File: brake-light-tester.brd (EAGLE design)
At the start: 47.2 x 62.2 mm, 24 parts, among them J1 CON_HEADER_PRG_AVR_ICSP-SMD, U1 ATTINY85-20SU, U2 TSL2561FN, U4 LM1117/5V

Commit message: Final version with silkscreens.
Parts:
- moved FID2 4.02 mm to (56.1, 28.9)
- moved FID1 1.27 mm to (22.9, 49.5)
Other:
- board text added: "(c) Chris von Csefalvay"
- board text added: "0x49 0x39 0x29"
- board text added: "BrakeDancer Mk I"
- board text added: "CR927 x 3"
- board text added: "Firmware"
- board text added: "Mfg: Date: S/N: Line: Batch: 20 19 18 17 16"

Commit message: Added drill legend.
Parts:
- added DRILEGEND: (no value), drilegend:DRILEGEND
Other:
- board text added: "01-16"
- board text added: "LAYER-STACK"
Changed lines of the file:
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@@
 <layer number="131" name="tAdjust" color="7" fill="1" visible="no" active="yes"/>
 <layer number="132" name="bAdjust" color="7" fill="1" visible="no" active="yes"/>
-<layer number="144" name="Drill_legend" color="7" fill="1" visible="no" active="yes"/>
+<layer number="144" name="DrillLegend" color="7" fill="1" visible="yes" active="yes"/>
+<layer number="145" name="DrillLegend_01-16" color="2" fill="9" visible="yes" active="yes"/>
 <layer number="150" name="Notes" color="7" fill="1" visible="no" active="yes"/>
 <layer number="151" name="HeatSink" color="7" fill="1" visible="no" active="yes"/>
@@
 <text x="46.99" y="15.24" size="0.6096" layer="122" font="vector" ratio="4">Firmware</text>
 <rectangle x1="41.91" y1="8.89" x2="55.88" y2="13.97" layer="122"/>
+<text x="-13.994165625" y="-10.905" size="0.6096" layer="144" font="vector" ratio="4">LAYER-STACK</text>
+<text x="-4.215165625" y="-13.8387" size="1.778" layer="145" font="vector" ratio="4">01-16</text>
+<wire x1="20.32" y1="29.718" x2="20.32" y2="28.702" width="0.1016" layer="145"/>
+<wire x1="19.812" y1="29.21" x2="20.828" y2="29.21" width="0.1016" layer="145"/>
+<wire x1="20.32" y1="37.338" x2="20.32" y2="36.322" width="0.1016" layer="145"/>
+<wire x1="19.812" y1="36.83" x2="20.828" y2="36.83" width="0.1016" layer="145"/>
+<wire x1="41.91" y1="39.878" x2="41.91" y2="38.862" width="0.1016" layer="145"/>
+<wire x1="41.402" y1="39.37" x2="42.418" y2="39.37" width="0.1016" layer="145"/>
+<wire x1="40.64" y1="48.768" x2="40.64" y2="47.752" width="0.1016" layer="145"/>
+<wire x1="40.132" y1="48.26" x2="41.148" y2="48.26" width="0.1016" layer="145"/>
+<wire x1="45.72" y1="36.068" x2="45.72" y2="35.052" width="0.1016" layer="145"/>
+<wire x1="45.212" y1="35.56" x2="46.228" y2="35.56" width="0.1016" layer="145"/>
+<wire x1="34.29" y1="34.798" x2="34.29" y2="33.782" width="0.1016" layer="145"/>
+<wire x1="33.782" y1="34.29" x2="34.798" y2="34.29" width="0.1016" layer="145"/>
+<wire x1="26.67" y1="37.338" x2="26.67" y2="36.322" width="0.1016" layer="145"/>
+<wire x1="26.162" y1="36.83" x2="27.178" y2="36.83" width="0.1016" layer="145"/>
+<wire x1="46.99" y1="30.988" x2="46.99" y2="29.972" width="0.1016" layer="145"/>
+<wire x1="46.482" y1="30.48" x2="47.498" y2="30.48" width="0.1016" layer="145"/>
+<wire x1="33.02" y1="36.068" x2="33.02" y2="35.052" width="0.1016" layer="145"/>
+<wire x1="32.512" y1="35.56" x2="33.528" y2="35.56" width="0.1016" layer="145"/>
+<wire x1="34.29" y1="47.498" x2="34.29" y2="46.482" width="0.1016" layer="145"/>
+<wire x1="33.782" y1="46.99" x2="34.798" y2="46.99" width="0.1016" layer="145"/>
+<wire x1="52.07" y1="24.638" x2="52.07" y2="23.622" width="0.1016" layer="145"/>
+<wire x1="51.562" y1="24.13" x2="52.578" y2="24.13" width="0.1016" layer="145"/>
+<wire x1="41.91" y1="28.448" x2="41.91" y2="27.432" width="0.1016" layer="145"/>
+<wire x1="41.402" y1="27.94" x2="42.418" y2="27.94" width="0.1016" layer="145"/>
+<wire x1="49.53" y1="24.638" x2="49.53" y2="23.622" width="0.1016" layer="145"/>
+<wire x1="49.022" y1="24.13" x2="50.038" y2="24.13" width="0.1016" layer="145"/>
+<wire x1="48.635684375" y1="27.178" x2="48.635684375" y2="26.162" width="0.1016" layer="145"/>
+<wire x1="48.127684375" y1="26.67" x2="49.143684375" y2="26.67" width="0.1016" layer="145"/>
+<wire x1="41.91" y1="43.688" x2="41.91" y2="42.672" width="0.1016" layer="145"/>
+<wire x1="41.402" y1="43.18" x2="42.418" y2="43.18" width="0.1016" layer="145"/>
+<wire x1="48.26" y1="42.418" x2="48.26" y2="41.402" width="0.1016" layer="145"/>
+<wire x1="47.752" y1="41.91" x2="48.768" y2="41.91" width="0.1016" layer="145"/>
+<wire x1="39.37" y1="33.528" x2="39.37" y2="32.512" width="0.1016" layer="145"/>
+<wire x1="38.862" y1="33.02" x2="39.878" y2="33.02" width="0.1016" layer="145"/>
+<wire x1="36.83" y1="46.228" x2="36.83" y2="45.212" width="0.1016" layer="145"/>
+<wire x1="36.322" y1="45.72" x2="37.338" y2="45.72" width="0.1016" layer="145"/>
+<wire x1="36.83" y1="33.528" x2="36.83" y2="32.512" width="0.1016" layer="145"/>
+<wire x1="36.322" y1="33.02" x2="37.338" y2="33.02" width="0.1016" layer="145"/>
+<wire x1="39.37" y1="55.118" x2="39.37" y2="54.102" width="0.1016" layer="145"/>
+<wire x1="38.862" y1="54.61" x2="39.878" y2="54.61" width="0.1016" layer="145"/>
+<wire x1="39.37" y1="34.798" x2="39.37" y2="33.782" width="0.1016" layer="145"/>
+<wire x1="38.862" y1="34.29" x2="39.878" y2="34.29" width="0.1016" layer="145"/>
+<wire x1="41.45579375" y1="32.45383125" x2="41.45579375" y2="31.43783125" width="0.1016" layer="145"/>
+<wire x1="40.94779375" y1="31.94583125" x2="41.96379375" y2="31.94583125" width="0.1016" layer="145"/>
+<wire x1="38.1" y1="53.848" x2="38.1" y2="52.832" width="0.1016" layer="145"/>
+<wire x1="37.592" y1="53.34" x2="38.608" y2="53.34" width="0.1016" layer="145"/>
+<wire x1="38.455309375" y1="38.761453125" x2="38.455309375" y2="37.745453125" width="0.1016" layer="145"/>
+<wire x1="37.947309375" y1="38.253453125" x2="38.963309375" y2="38.253453125" width="0.1016" layer="145"/>
+<wire x1="30.48" y1="41.148" x2="30.48" y2="40.132" width="0.1016" layer="145"/>
+<wire x1="29.972" y1="40.64" x2="30.988" y2="40.64" width="0.1016" layer="145"/>
+<wire x1="27.94" y1="41.148" x2="27.94" y2="40.132" width="0.1016" layer="145"/>
+<wire x1="27.432" y1="40.64" x2="28.448" y2="40.64" width="0.1016" layer="145"/>
+<wire x1="22.352" y1="56.388" x2="23.368" y2="55.372" width="0.1016" layer="145"/>
+<wire x1="23.368" y1="56.388" x2="22.352" y2="55.372" width="0.1016" layer="145"/>
+<wire x1="27.432" y1="6.858" x2="28.448" y2="5.842" width="0.1016" layer="145"/>
+<wire x1="28.448" y1="6.858" x2="27.432" y2="5.842" width="0.1016" layer="145"/>
 </plain>
 <attributes>
@@
 <attribute name="VALUE" x="23.495" y="28.194" size="0.4064" layer="27" ratio="10" rot="R270"/>
 </element>
+<element name="DRILEGEND" library="drilegend" package="DRILEGEND" value="" x="4.67484375" y="-10.90500625"/>
 </elements>
 <signals>

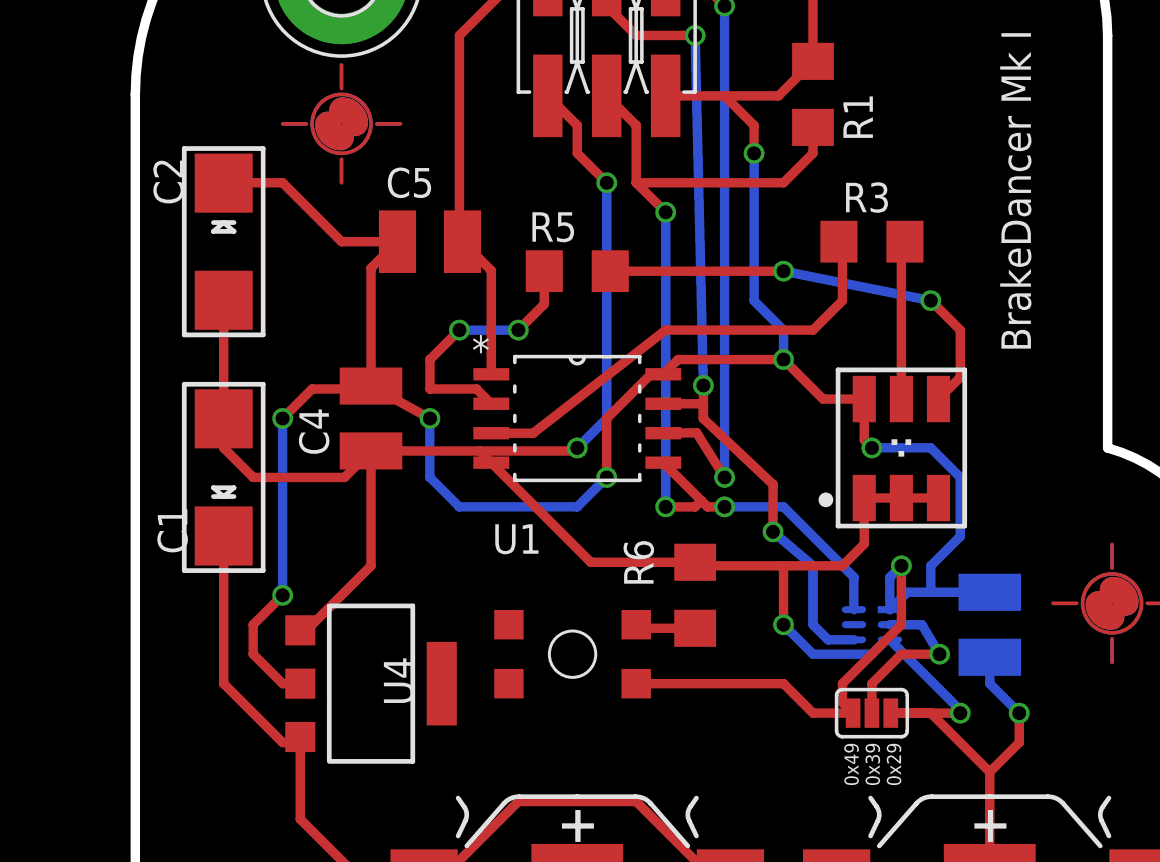
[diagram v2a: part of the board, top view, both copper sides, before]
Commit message: Replaced 1210 caps with 1206s as they are much more available.
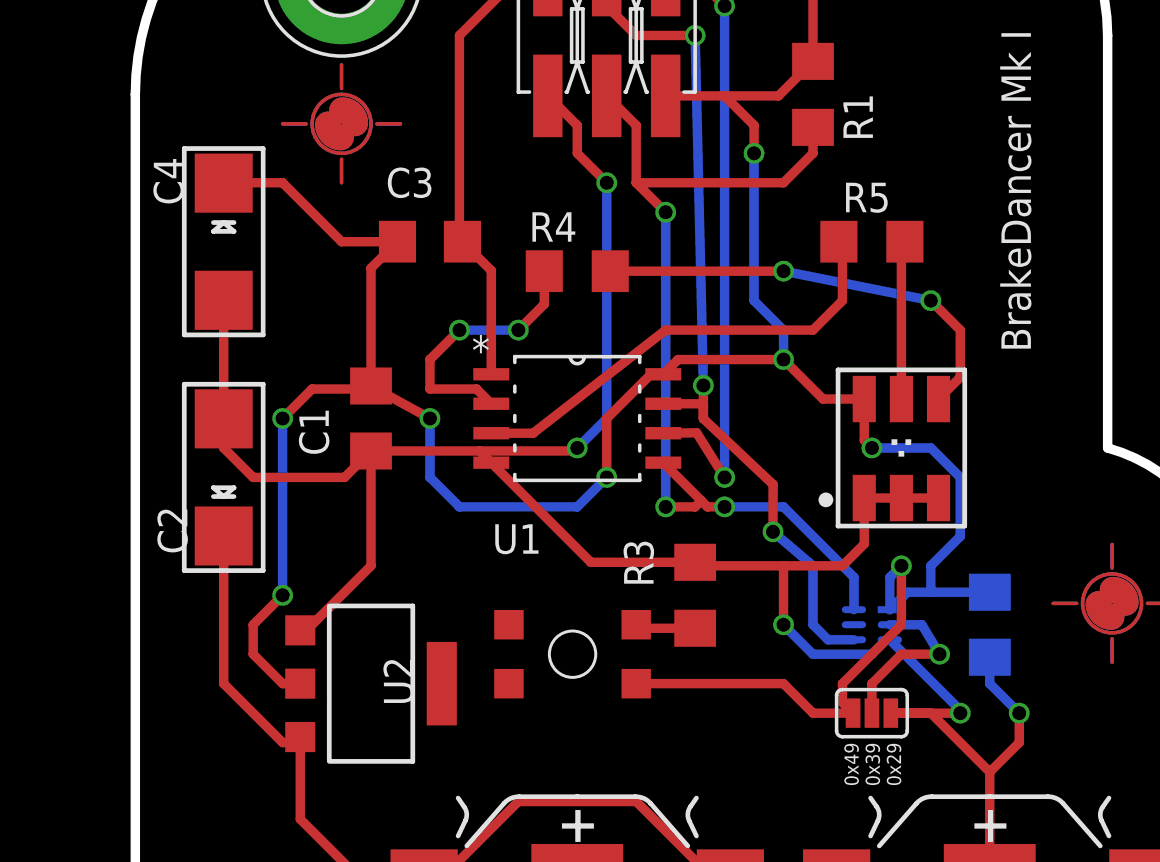
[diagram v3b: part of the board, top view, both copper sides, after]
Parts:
- removed R6: 10k, rcl:R1206
- removed U4: LM1117/5V, microbuilder:SOT223-R
- added R4: 68R, rcl:R1206
- added U3: TSL2561FN, SparkFun-DigitalIC:FN-6
- C1: value 10uF -> 0.1uF; device microbuilder:EIA6032-28/C-R -> rcl:C1206
- C3, C5: device rcl:C1210 -> rcl:C1206
- C4: value 0.1uF -> 10uF; device rcl:C1210 -> microbuilder:EIA6032-28/C-R
- R3: value 56R -> 10k
- R5: value 68R -> 56R
- U2: value TSL2561FN -> LM1117/5V; device SparkFun-DigitalIC:FN-6 -> microbuilder:SOT223-R
- moved FID1 39.1 mm to (56.1, 28.9)
- moved FID2 39.1 mm to (22.9, 49.5)
- moved C3 29.2 mm to (26.7, 44.5), flipped to the top, turned to 0 degrees
- moved C5 29.2 mm to (50.8, 27.9), flipped to the bottom, turned to 270 degrees
- moved U2 21.7 mm to (24.1, 25.4), flipped to the top, turned to 270 degrees
- moved R3 17.0 mm to (38.1, 29.2), turned to 90 degrees
- moved R5 12.8 mm to (45.7, 44.5), turned to 0 degrees
- moved C2 10.2 mm to (17.8, 34.3), turned to 270 degrees
- moved C4 9.92 mm to (17.8, 44.5), turned to 90 degrees
- moved C1 6.84 mm to (24.1, 36.8)
- renumbered U$2 to SW1
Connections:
- net +5V: now also C1.1, C4.+, U2.2, U3.1; no longer C2.+, C4.1, U2.1, U4.2
- net GND: now also C1.2, C4.-, C5.2, R3.2, U2.1, U3.3; no longer C1.-, C3.2, C4.2, R6.2, U2.3, U4.1
- net N$1: now also C2.+, U2.3; no longer C1.+, U4.3
- net N$2: now also U3.2; no longer U2.2
- net N$3: now also R4.1; no longer R5.1
- net N$4: now also R5.2; no longer R3.2
- net N$7: now also R3.1; no longer R6.1
- net PB0: now also U3.6; no longer U2.6
- net PB2: now also U3.4; no longer U2.4
- net PB3: now also R4.2; no longer R5.2
- net PB4: now also R5.1; no longer R3.1
- net PB5: now also C3.2; no longer C5.2
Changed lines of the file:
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@@
 </autorouter>
 <elements>
-<element name="C1" library="microbuilder" package="EIA6032-28/C-R" value="10uF" x="17.78" y="34.29" smashed="yes" rot="R270">
+<element name="C2" library="microbuilder" package="EIA6032-28/C-R" value="10uF" x="17.78" y="34.29" smashed="yes" rot="R270">
 <attribute name="NAME" x="14.941965625" y="33.06193125" size="1.27" layer="25" font="vector" ratio="4" rot="R270"/>
 <attribute name="VALUE" x="17.143" y="29.924" size="0.4064" layer="27" ratio="10" rot="R270"/>
 </element>
-<element name="C2" library="microbuilder" package="EIA6032-28/C-R" value="10uF" x="17.78" y="44.45" smashed="yes" rot="R90">
+<element name="C4" library="microbuilder" package="EIA6032-28/C-R" value="10uF" x="17.78" y="44.45" smashed="yes" rot="R90">
 <attribute name="NAME" x="16.039096875" y="46.010878125" size="1.27" layer="25" font="vector" ratio="4" rot="R90"/>
 <attribute name="VALUE" x="18.417" y="48.816" size="0.4064" layer="27" ratio="10" rot="R90"/>
 </element>
-<element name="C3" library="rcl" package="C1210" value="0.1uF" x="50.8" y="27.94" smashed="yes" rot="MR270">
+<element name="C5" library="rcl" package="C1206" value="0.1uF" x="50.8" y="27.94" smashed="yes" rot="MR270">
 <attribute name="NAME" x="48.895" y="29.845" size="1.27" layer="26" font="vector" ratio="4" rot="MR270"/>
 <attribute name="VALUE" x="53.975" y="29.845" size="1.27" layer="28" rot="MR270"/>
 </element>
-<element name="C4" library="rcl" package="C1210" value="0.1uF" x="24.13" y="36.83" smashed="yes" rot="R270">
+<element name="C1" library="rcl" package="C1206" value="0.1uF" x="24.13" y="36.83" smashed="yes" rot="R270">
 <attribute name="NAME" x="21.04200625" y="37.308665625" size="1.27" layer="25" font="vector" ratio="4" rot="R270"/>
 <attribute name="VALUE" x="20.955" y="38.735" size="1.27" layer="27" rot="R270"/>
 </element>
-<element name="C5" library="rcl" package="C1210" value="0.1uF" x="26.67" y="44.45" smashed="yes">
+<element name="C3" library="rcl" package="C1206" value="0.1uF" x="26.67" y="44.45" smashed="yes">
 <attribute name="NAME" x="24.765" y="46.355" size="1.27" layer="25" font="vector" ratio="4"/>
 <attribute name="VALUE" x="24.765" y="41.275" size="1.27" layer="27"/>
 </element>
-<element name="FID1" library="microbuilder" package="PASS-ROUND" value="FIDUCIALROUND" x="22.86" y="49.53" smashed="yes"/>
-<element name="FID2" library="microbuilder" package="PASS-ROUND" value="FIDUCIALROUND" x="56.071815625" y="28.8608625" smashed="yes"/>
+<element name="FID2" library="microbuilder" package="PASS-ROUND" value="FIDUCIALROUND" x="22.86" y="49.53" smashed="yes"/>
+<element name="FID1" library="microbuilder" package="PASS-ROUND" value="FIDUCIALROUND" x="56.071815625" y="28.8608625" smashed="yes"/>
 <element name="G1" library="battery" package="10MM_SM_COIN_CELL_CLIP" value="10MM_SM_COIN_CELL_CLIP" x="50.8" y="16.51" smashed="yes">
 <attribute name="VALUE" x="46.31745" y="10.07065" size="1.27" layer="27" font="vector"/>
@@
 <attribute name="VALUE" x="40.64" y="58.42" size="1.27" layer="27" rot="R270"/>
 </element>
-<element name="R3" library="rcl" package="R1206" value="56R" x="45.72" y="44.45" smashed="yes">
+<element name="R5" library="rcl" package="R1206" value="56R" x="45.72" y="44.45" smashed="yes">
 <attribute name="NAME" x="44.45" y="45.72" size="1.27" layer="25" font="vector" ratio="4"/>
 <attribute name="VALUE" x="44.45" y="41.91" size="1.27" layer="27"/>
 </element>
-<element name="R5" library="rcl" package="R1206" value="68R" x="33.02" y="43.18" smashed="yes" rot="R180">
+<element name="R4" library="rcl" package="R1206" value="68R" x="33.02" y="43.18" smashed="yes" rot="R180">
 <attribute name="NAME" x="33.02" y="45.72" size="1.27" layer="25" font="vector" ratio="4" rot="R180"/>
 <attribute name="VALUE" x="34.29" y="45.72" size="1.27" layer="27" rot="R180"/>
 </element>
-<element name="R6" library="rcl" package="R1206" value="10k" x="38.1" y="29.21" smashed="yes" rot="R90">
+<element name="R3" library="rcl" package="R1206" value="10k" x="38.1" y="29.21" smashed="yes" rot="R90">
 <attribute name="NAME" x="36.306925" y="29.5565125" size="1.27" layer="25" font="vector" ratio="4" rot="R90"/>
 <attribute name="VALUE" x="40.64" y="27.94" size="1.27" layer="27" rot="R90"/>
@@
 <attribute name="VALUE" x="44.45" y="22.225" size="0.4064" layer="27"/>
 </element>
-<element name="U$2" library="GeekAmmo" package="7914G" value="TACTILE-SWITCH-7914G" x="35.56" y="25.4" smashed="yes" rot="R90">
+<element name="SW1" library="GeekAmmo" package="7914G" value="TACTILE-SWITCH-7914G" x="35.56" y="25.4" smashed="yes" rot="R90">
 <attribute name="VALUE" x="35.56" y="30.48" size="0.8128" layer="27" rot="R180"/>
 </element>
@@
 <attribute name="VALUE" x="29.5656" y="41.91" size="2.0828" layer="27" ratio="10" rot="SR0"/>
 </element>
-<element name="U2" library="SparkFun-DigitalIC" package="FN-6" value="TSL2561FN" x="45.72" y="27.94" smashed="yes" rot="MR0">
+<element name="U3" library="SparkFun-DigitalIC" package="FN-6" value="TSL2561FN" x="45.72" y="27.94" smashed="yes" rot="MR0">
 <attribute name="PROD_ID" value="IC-11791" x="45.72" y="27.94" size="1.778" layer="28" rot="MR0" display="off"/>
 <attribute name="NAME" x="45.72" y="29.19" size="1.27" layer="26" font="vector" ratio="4" rot="MR0" align="bottom-center"/>
 <attribute name="VALUE" x="45.72" y="26.69" size="0.4064" layer="28" rot="MR180" align="bottom-center"/>
 </element>
-<element name="U4" library="microbuilder" package="SOT223-R" value="LM1117/5V" x="24.13" y="25.4" smashed="yes" rot="R270">
+<element name="U2" library="microbuilder" package="SOT223-R" value="LM1117/5V" x="24.13" y="25.4" smashed="yes" rot="R270">
 <attribute name="NAME" x="24.684971875" y="26.5774875" size="1.27" layer="25" font="vector" ratio="4" rot="R270"/>
 <attribute name="VALUE" x="23.495" y="28.194" size="0.4064" layer="27" ratio="10" rot="R270"/>
@@
 <signal name="GND">
 <contactref element="U1" pad="4"/>
-<contactref element="C4" pad="2"/>
-<contactref element="U2" pad="3"/>
-<contactref element="C1" pad="-"/>
+<contactref element="C1" pad="2"/>
+<contactref element="U3" pad="3"/>
 <contactref element="C2" pad="-"/>
-<contactref element="U4" pad="1"/>
+<contactref element="C4" pad="-"/>
+<contactref element="U2" pad="1"/>
 <contactref element="LED1" pad="3"/>
 <contactref element="LED1" pad="2"/>
 <contactref element="LED1" pad="1"/>
-<contactref element="R6" pad="2"/>
+<contactref element="R3" pad="2"/>
 <contactref element="SJ1" pad="3"/>
-<contactref element="C3" pad="2"/>
+<contactref element="C5" pad="2"/>
 <contactref element="G1" pad="-"/>
 <contactref element="J1" pad="6"/>
@@
 </signal>
 <signal name="PB0">
-<contactref element="U2" pad="6"/>
+<contactref element="U3" pad="6"/>
 <contactref element="R1" pad="1"/>
 <contactref element="U1" pad="5"/>
@@
 </signal>
 <signal name="PB2">
-<contactref element="U2" pad="4"/>
+<contactref element="U3" pad="4"/>
 <contactref element="R2" pad="1"/>
 <contactref element="U1" pad="7"/>
@@
 </signal>
 <signal name="PB3">
-<contactref element="R5" pad="2"/>
+<contactref element="R4" pad="2"/>
 <contactref element="U1" pad="2"/>
 <wire x1="31.598" y1="43.18" x2="31.598" y2="41.758" width="0.4064" layer="1"/>
@@
 </signal>
 <signal name="PB4">
-<contactref element="R3" pad="1"/>
+<contactref element="R5" pad="1"/>
 <contactref element="U1" pad="3"/>
 <wire x1="29.3116" y1="36.195" x2="31.115" y2="36.195" width="0.4064" layer="1"/>
@@
 <signal name="PB5">
 <contactref element="U1" pad="1"/>
-<contactref element="C5" pad="2"/>
+<contactref element="C3" pad="2"/>
 <contactref element="J1" pad="5"/>
 <wire x1="28.07" y1="44.45" x2="29.3116" y2="43.2084" width="0.4064" layer="1"/>
@@
 <signal name="N$2">
 <contactref element="SJ1" pad="2"/>
-<contactref element="U2" pad="2"/>
+<contactref element="U3" pad="2"/>
 <via x="48.635684375" y="26.67" extent="1-16" drill="0.6" shape="square"/>
 <wire x1="48.635684375" y1="26.67" x2="47.872578125" y2="27.94" width="0.4064" layer="16"/>
@@
 </signal>
 <signal name="N$1">
-<contactref element="U4" pad="3"/>
-<contactref element="C1" pad="+"/>
+<contactref element="U2" pad="3"/>
+<contactref element="C2" pad="+"/>
 <contactref element="G3" pad="+@1"/>
 <contactref element="G3" pad="+@2"/>
@@
 <signal name="N$3">
 <contactref element="LED1" pad="4"/>
-<contactref element="R5" pad="1"/>
+<contactref element="R4" pad="1"/>
 <wire x1="34.442" y1="43.18" x2="41.91" y2="43.18" width="0.4064" layer="1"/>
 <via x="41.91" y="43.18" extent="1-16" drill="0.6" shape="square"/>
@@
 </signal>
 <signal name="N$4">
-<contactref element="R3" pad="2"/>
+<contactref element="R5" pad="2"/>
 <contactref element="LED1" pad="5"/>
 <wire x1="47.142" y1="44.45" x2="46.99" y2="44.298" width="0.4064" layer="1"/>
@@
 </signal>
 <signal name="N$7">
-<contactref element="U$2" pad="3"/>
-<contactref element="R6" pad="1"/>
+<contactref element="SW1" pad="3"/>
+<contactref element="R3" pad="1"/>
 <wire x1="35.56" y1="27.94" x2="35.712" y2="27.788" width="0.4064" layer="1"/>
 <wire x1="35.712" y1="27.788" x2="38.1" y2="27.788" width="0.4064" layer="1"/>
 </signal>
 <signal name="+5V">
-<contactref element="U4" pad="2"/>
-<contactref element="C2" pad="+"/>
-<contactref element="U$2" pad="1"/>
-<contactref element="C5" pad="1"/>
-<contactref element="C4" pad="1"/>
+<contactref element="U2" pad="2"/>
+<contactref element="C4" pad="+"/>
+<contactref element="SW1" pad="1"/>
+<contactref element="C3" pad="1"/>
+<contactref element="C1" pad="1"/>
 <contactref element="U1" pad="8"/>
 <contactref element="R2" pad="2"/>
 <contactref element="R1" pad="2"/>
 <contactref element="LED1" pad="6"/>
-<contactref element="U2" pad="1"/>
+<contactref element="U3" pad="1"/>
 <contactref element="SJ1" pad="1"/>
-<contactref element="C3" pad="1"/>
+<contactref element="C5" pad="1"/>
 <contactref element="J1" pad="2"/>
 <wire x1="35.56" y1="25.4" x2="41.91" y2="25.4" width="0.4064" layer="1"/>
